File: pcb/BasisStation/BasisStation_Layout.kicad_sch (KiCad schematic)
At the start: 23 parts, among them J5 Conn_02x05_Odd_Even, J6 Conn_02x03_Odd_Even, Q1 BC337, Q2 BC337, Q3 BC337, Q4 BC337, U6 ESP32-S3-WROOM-1U-N16R8

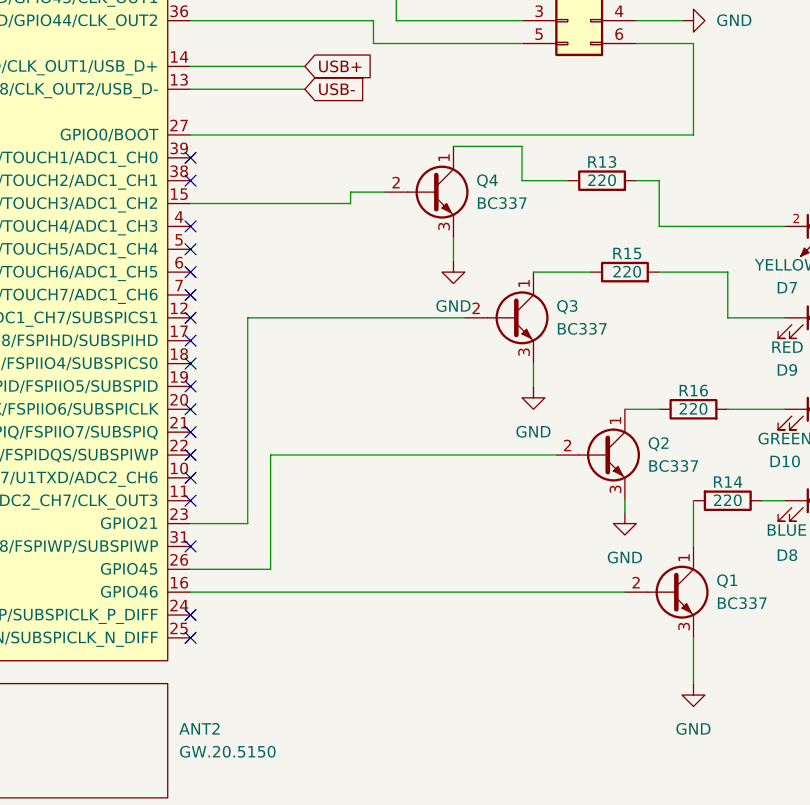
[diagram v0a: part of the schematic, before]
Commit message: v0.00.001 fix(SHBS-9): LED-Treiber Q1-Q4 mit Basiswiderstaenden und unkritischen GPIOs
Die Treiberstufen der vier Status-LEDs hingen ohne Basisvorwiderstand
direkt an den GPIO-Pins des ESP32-S3. Die Basis-Emitter-Strecke klemmt
den Pin auf ca. 0,7 V, sodass der Pin-Strom nur durch die
Treiberimpedanz begrenzt wurde.

- R23-R26 (4,7 kOhm) zwischen GPIO und Basis ergaenzt, Basisstrom nun
  ca. 0,55 mA je Zweig
- LEDs von den Strapping-Pins GPIO3/45/46 auf GPIO21/38/47/48 umgelegt;
  diese haben keine Strapping-, ADC- oder Touch-Funktion
- GPIO3, GPIO45 und GPIO46 sind damit frei, GPIO35-37 bleiben fuer das
  Octal-PSRAM des Moduls N16R8 unbeschaltet

ERC: 0 Fehler, 9 Warnungen (unveraendert zum Stand vor der Aenderung).

Co-Authored-By: Claude Opus 5 <noreply@anthropic.com>
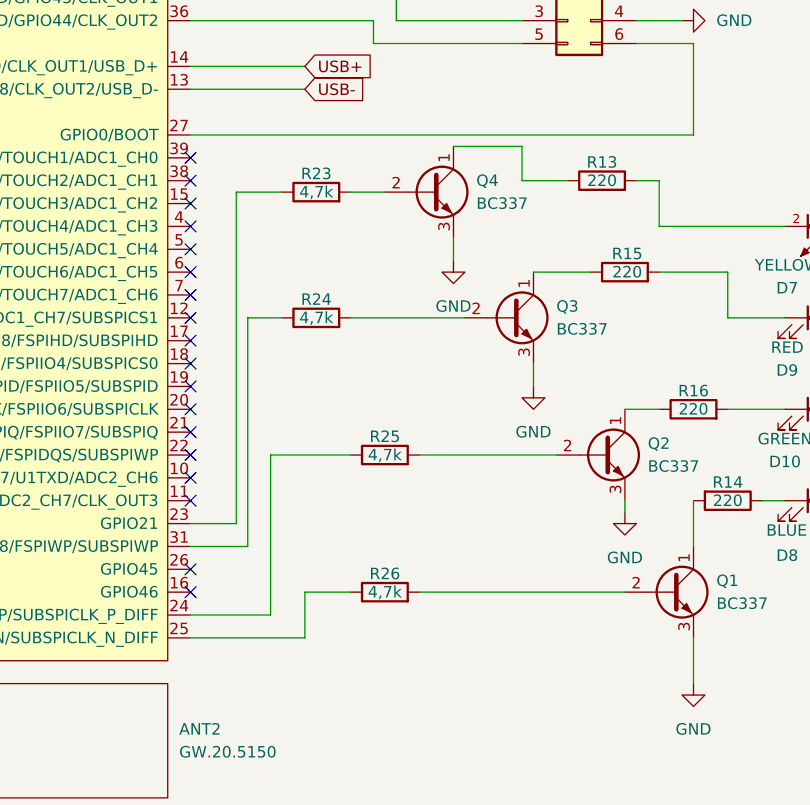
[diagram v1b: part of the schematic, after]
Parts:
- added R23, R24, R25, R26: 4,7k, Resistor_THT:R_Axial_DIN0617_L17.0mm_D6.0mm_P20.32mm_Horizontal, symbol Device:R
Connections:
- net at Q1.2 (B): now also R26.2; no longer U6.16 (GPIO46)
- net at Q4.2 (B): now also R23.2; no longer U6.15 (GPIO3/TOUCH3/ADC1_CH2)
- net at U6.23 (GPIO21): now also R23.1; no longer Q3.2 (B)
- net at U6.24 (GPIO47/SPICLK_P/SUBSPICLK_P_DIFF): now also R25.1
- net at U6.25 (GPIO48/SPICLK_N/SUBSPICLK_N_DIFF): now also R26.1
- net at U6.26 (GPIO45): no longer Q2.2 (B)
- net at U6.31 (GPIO38/FSPIWP/SUBSPIWP): now also R24.1
- new net: Q3.2 (B), R24.2
- new net: Q2.2 (B), R25.2

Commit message: v0.00.001 refactor(SHBS-12): KiCad-Bibliotheken auf Bauteilordner umgestellt
Symbol, Footprint und 3D-Modell eines Bauteils lagen bisher in drei
getrennten Sammelordnern. Jedes Bauteil hat jetzt einen eigenen Ordner
unter pcb/Bauteile/; pcb/Symbol/, pcb/Footprints/ und pcb/3D-Model/
entfallen.

Umfang: 20 Dateien verschoben, 13 verwaiste entfernt, 63 Footprint-
Referenzen in Schaltplaenen, Netzliste und Board umgeschrieben, 7
Footprint-Vorgaben in den Symbol-Dateien angepasst.

Nebenbei behoben:
- Die 3D-Modelle waren im Board ueber absolute Pfade auf E: und in der
  Netzliste auf C: verdrahtet, funktionsfaehig jeweils nur auf einem
  Rechner. Jetzt durchgaengig ueber ${KIPRJMOD}.
- Drei Footprint-Referenzen zeigten auf Bibliotheken, die nie in der
  fp-lib-table standen.
- WCAP-FTXX_P10 hatte keine Footprint-Vorgabe, der W5500-Footprint keine
  3D-Referenz.
- fp-info-cache und *.kicad_prl sind nicht mehr versioniert.

Verifikation: Projekt oeffnet ohne Bibliotheks-Warnung. ERC 0 Fehler und
7 Warnungen, vorher 9, keine neue. DRC meldet "Found 0 Footprint errors";
der verbliebene DRC-Fehler ist eine vorbestehende Routing-Luecke im
EN-Netz. 3D-Ansicht zeigt die Modelle.

Co-Authored-By: Claude Opus 5 <noreply@anthropic.com>
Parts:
- C10, C12, C7: footprint Footprints:WCAP-FTXX_P10L13W7H13 -> WCAP-FTXX_P10:WCAP-FTXX_P10L13W7H13
- C8: footprint Footprints:WCAP-PT5H_6.3X5.2_DXL_ -> WCAP-PT5H_6.3X5.2:WCAP-PT5H_6.3X5.2_DXL_
- D10, D7: footprint Footprints:WL-TMRC_3MM -> WL-TMRC_3MM:WL-TMRC_3MM
- D8, D9: footprint Footprints:WL-TMRW_3MM -> WL-TMRW_3MM:WL-TMRW_3MM
- J5: footprint Footprints:61201021621 -> wuerth_6120XX21621:61201021621
- J6: footprint Footprints:61200621621 -> wuerth_6120XX21621:61200621621
- S2: footprint Footprints:1543650149 -> 1543-650-149:1543650149
- U6: footprint Footprints:ESP32-S3-WROOM-1U -> ESP32-S3-WROOM-1U-N16R8:ESP32-S3-WROOM-1U
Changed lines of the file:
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@@
 			)
 		)
-		(property "Footprint" "Footprints:WL-TMRW_3MM"
+		(property "Footprint" "WL-TMRW_3MM:WL-TMRW_3MM"
 			(at 254 96.52 0)
 			(effects
@@
 			)
 		)
-		(property "Footprint" "Footprints:WCAP-FTXX_P10L13W7H13"
+		(property "Footprint" "WCAP-FTXX_P10:WCAP-FTXX_P10L13W7H13"
 			(at 146.05 41.91 0)
 			(effects
@@
 			)
 		)
-		(property "Footprint" "Footprints:WL-TMRC_3MM"
+		(property "Footprint" "WL-TMRC_3MM:WL-TMRC_3MM"
 			(at 252.73 86.36 0)
 			(effects
@@
 			)
 		)
-		(property "Footprint" "Footprints:WCAP-PT5H_6.3X5.2_DXL_"
+		(property "Footprint" "WCAP-PT5H_6.3X5.2:WCAP-PT5H_6.3X5.2_DXL_"
 			(at 66.04 30.48 0)
 			(effects
@@
 			)
 		)
-		(property "Footprint" "Footprints:WL-TMRW_3MM"
+		(property "Footprint" "WL-TMRW_3MM:WL-TMRW_3MM"
 			(at 254 116.84 0)
 			(effects
@@
 			)
 		)
-		(property "Footprint" "Footprints:WCAP-FTXX_P10L13W7H13"
+		(property "Footprint" "WCAP-FTXX_P10:WCAP-FTXX_P10L13W7H13"
 			(at 57.15 68.58 0)
 			(effects
@@
 			)
 		)
-		(property "Footprint" "Footprints:WL-TMRC_3MM"
+		(property "Footprint" "WL-TMRC_3MM:WL-TMRC_3MM"
 			(at 254 106.68 0)
 			(effects
@@
 			)
 		)
-		(property "Footprint" "Footprints:1543650149"
+		(property "Footprint" "1543-650-149:1543650149"
 			(at 57.15 60.96 0)
 			(effects
@@
 			)
 		)
-		(property "Footprint" "Footprints:ESP32-S3-WROOM-1U"
+		(property "Footprint" "ESP32-S3-WROOM-1U-N16R8:ESP32-S3-WROOM-1U"
 			(at 140.97 144.78 0)
 			(effects
@@
 			)
 		)
-		(property "Footprint" "Footprints:WCAP-FTXX_P10L13W7H13"
+		(property "Footprint" "WCAP-FTXX_P10:WCAP-FTXX_P10L13W7H13"
 			(at 247.65 45.72 0)
 			(effects
@@
 			)
 		)
-		(property "Footprint" "Footprints:61200621621"
+		(property "Footprint" "wuerth_6120XX21621:61200621621"
 			(at 226.06 63.5 0)
 			(effects
@@
 			)
 		)
-		(property "Footprint" "Footprints:61201021621"
+		(property "Footprint" "wuerth_6120XX21621:61201021621"
 			(at 46.99 97.79 0)
 			(effects

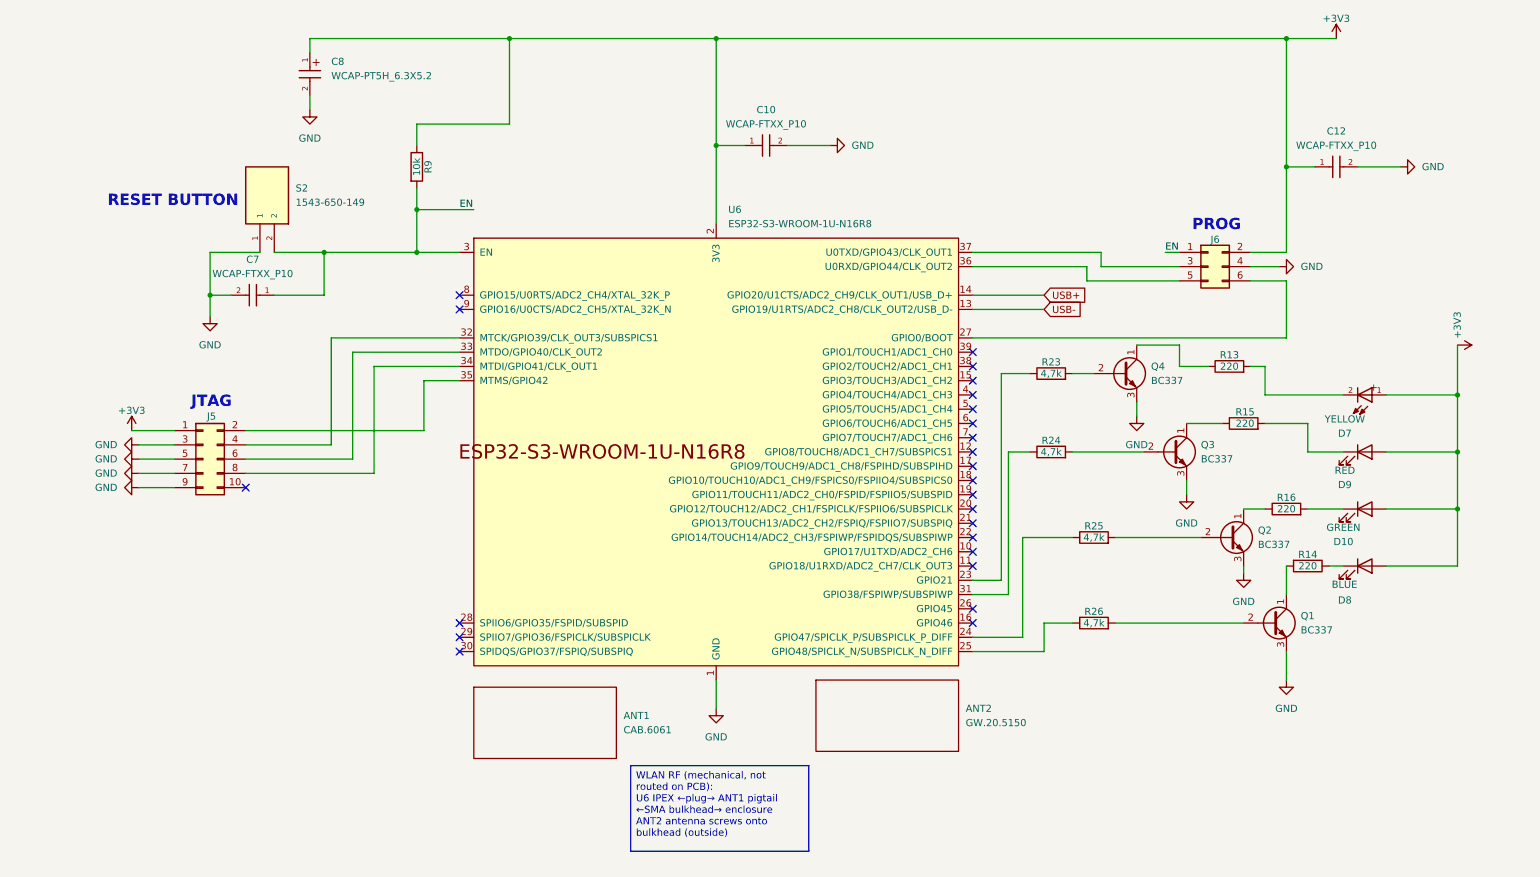
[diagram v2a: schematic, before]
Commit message: v0.00.001 fix(SHBS-6): Debugging-Blatt wiederhergestellt, JTAG-Header entfaellt
Das Blatt BasisStation_Debugging.kicad_sch war beim Anlegen des neuen
Ethernet-Blatts ueberschrieben worden und enthielt nur noch einen leeren
Rumpf. Aus dem letzten Commit zurueckgeholt; J1, U1, R21 und R22 sind
wieder da. Die interne UUID stimmt mit der Referenz im Wurzelblatt
ueberein, die Annotation bleibt damit erhalten.

Der 10-polige JTAG-Header J5 wurde bewusst entfernt: Der ESP32-S3 bringt
USB-Serial-JTAG im Chip mit, On-Chip-Debugging laeuft ueber J1. Das spart
einen Steckverbinder und dessen Platinenflaeche.

Doku nachgezogen: Schnittstellentabelle in hardware.md, Begruendung der
LED-Pinwahl (GPIO3 bleibt aus Strapping-Gruenden unbelegt, auch ohne J5),
sowie der GPIO-Ausschluss in Task 0003.

Offen: Das Board enthaelt den Footprint von J5 noch, er verschwindet beim
naechsten Netzlisten-Import.

Co-Authored-By: Claude Opus 5 <noreply@anthropic.com>
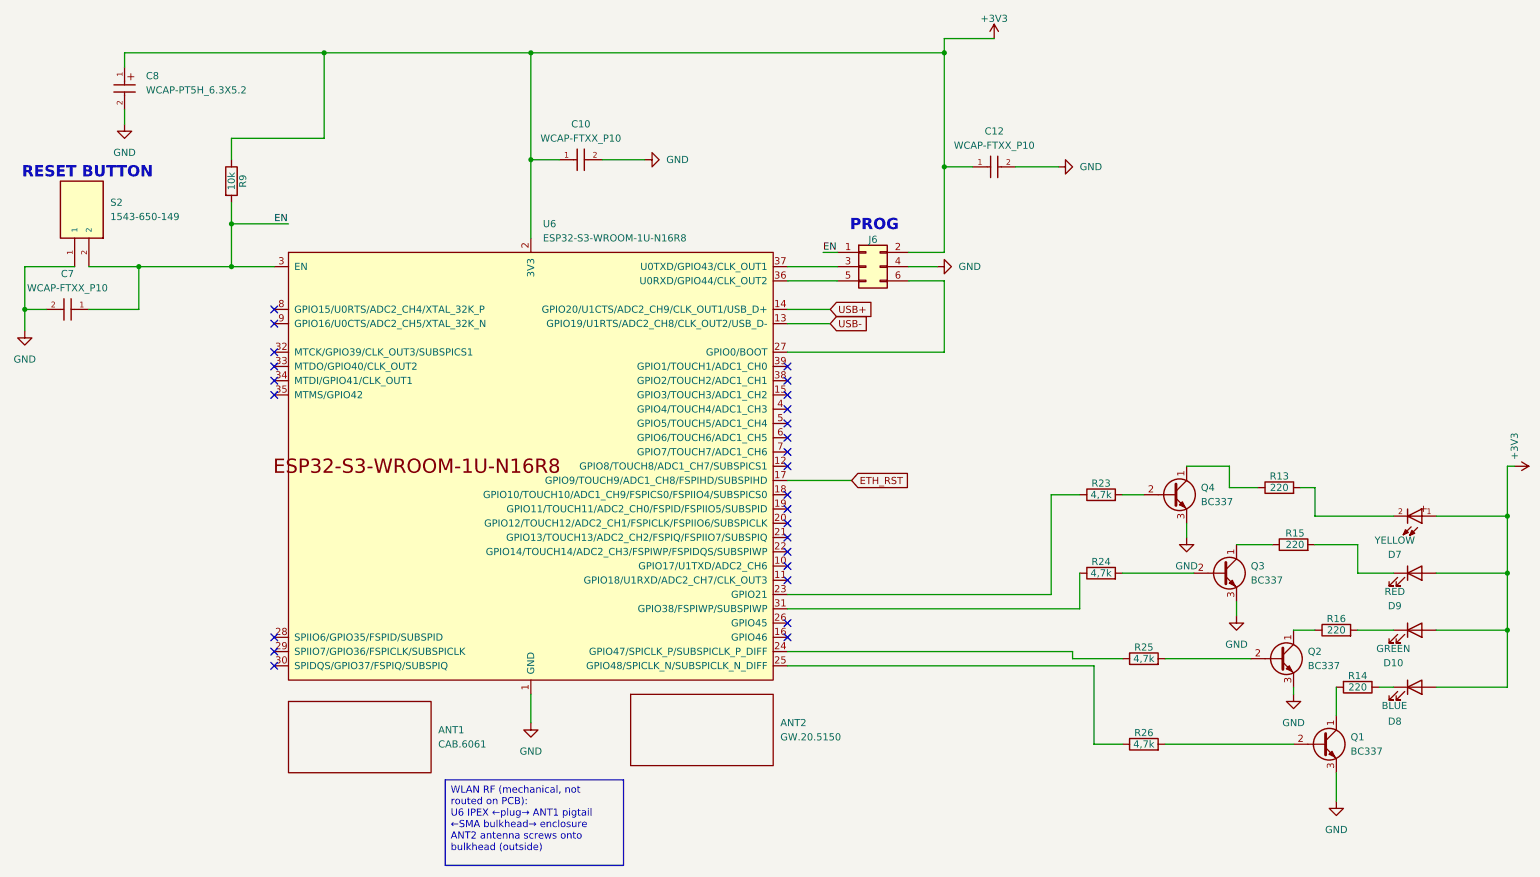
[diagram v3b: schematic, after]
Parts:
- removed J5: Conn_02x05_Odd_Even, wuerth_6120XX21621:61201021621, symbol Connector_Generic:Conn_02x05_Odd_Even
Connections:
- net ETH_RST: now reaches U6.17 (GPIO9/TOUCH9/ADC1_CH8/FSPIHD/SUBSPIHD)
- no-connect marks 24 -> 26
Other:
- note removed: "JTAG"
- moved on the sheet: ANT1, ANT2, C10, C12, C7, C8, D10, D7, D8, D9, J6, Q1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
